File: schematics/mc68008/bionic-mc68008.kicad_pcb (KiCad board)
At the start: 2 copper layers, 66 x 71.1 mm, 16 parts, among them J1 Bionic-P135, J1 BionicConnector, J2 Bionic-P245, U1 MC68008P, U2 74HCT126, U3 74HCT541, U4 74HCT541, U5 11AA010-I/TO

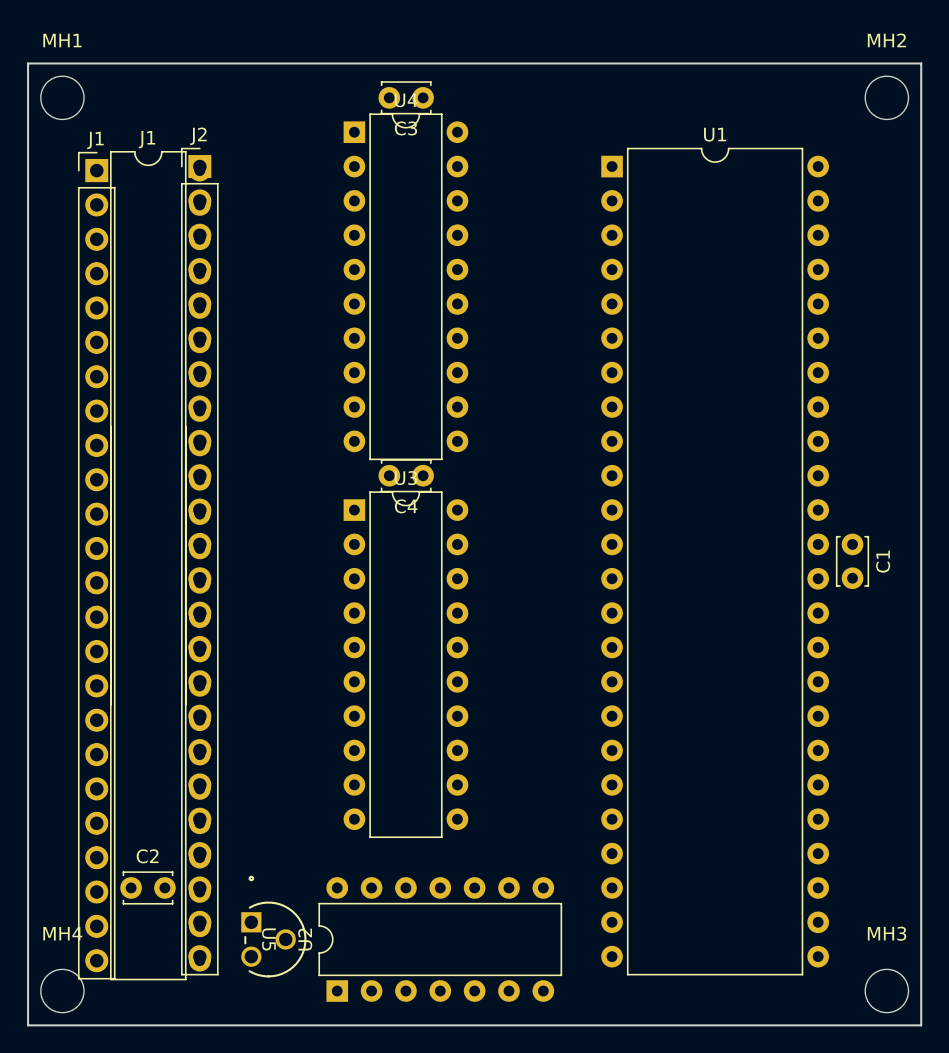
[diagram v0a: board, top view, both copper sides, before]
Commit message: [WIP] [MC68008] Update schematics
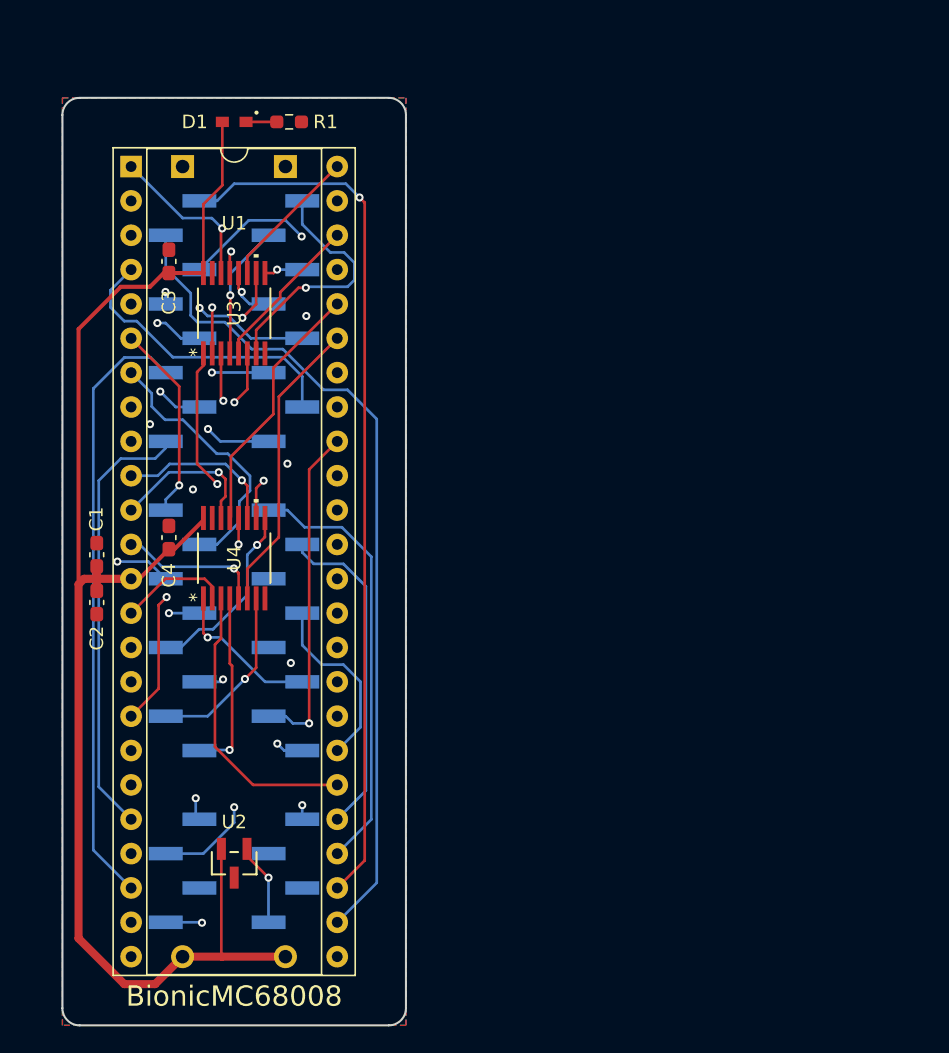
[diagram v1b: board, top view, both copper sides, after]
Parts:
- removed the J1 at (103.5, 75.4) (x2)
- removed MH1, MH2, MH3, MH4: MountingHole_3.2mm_M3, MountingHole:MountingHole_3.2mm_M3
- removed U5: 11AA010-I/TO, microchip:TO-92_MC_MCH
- added D1: CSL1901UW1, rhom:LED_CSL1901UW1_ROM-M, F.Cu at (113.7, 71.8)
- added J1: Bionic-P135, bionic:Bionic-P135_SMT, B.Cu at (109.9, 104.3)
- added R1: 1.6k, Resistor_SMD:R_0603_1608Metric_Pad0.98x0.95mm_HandSolder, F.Cu at (117.8, 71.8)
- C1, C3, C4: footprint Capacitor_THT:C_Disc_D3.4mm_W2.1mm_P2.50mm -> Capacitor_SMD:C_0603_1608Metric_Pad1.08x0.95mm_HandSolder
- C2: value 0.1u -> 22u; footprint Capacitor_THT:C_Disc_D3.4mm_W2.1mm_P2.50mm -> Capacitor_SMD:C_0603_1608Metric_Pad1.08x0.95mm_HandSolder
- J2: footprint connector:Bionic-P245_Vertical -> bionic:Bionic-P245_SMT; moved to B.Cu
- U1: footprint Package_DIP:DIP-48_W15.24mm -> bionic:DIP-48_W15.24mm_Socket
- U2: value 74HCT126 -> 11AA010-I/TT; footprint Package_DIP:DIP-14_W7.62mm -> microchip:SOT-23_MC_MCH-M
- U3, U4: value 74HCT541 -> 74AHCT157; footprint Package_DIP:DIP-20_W7.62mm -> ti:PW16-M
- moved C1 55.9 mm to (103.5, 103.8), turned to 90 degrees
- moved U1 35.6 mm to (106.1, 75.1)
- moved U4 32.7 mm to (113.7, 104.0), turned to 90 degrees
- moved J2 29.9 mm to (117.5, 104.3), turned to 180 degrees
- moved C3 22.3 mm to (108.9, 82.1), turned to 90 degrees
- moved C2 21.3 mm to (103.5, 107.3), turned to -90 degrees
- moved C4 19.3 mm to (108.9, 102.5), turned to 90 degrees
- moved U3 17.1 mm to (113.7, 85.9), turned to 90 degrees
- moved U2 12.1 mm to (113.7, 126.6), turned to 180 degrees
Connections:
- net Net-(U1-A17) renamed /A17
- J2 pad 28: /P55 -> unconnected-(J2-P55-Pad28)
- J2 pad 34: /P44 -> unconnected-(J2-P44-Pad34)
- J2 pad 36: /P42 -> unconnected-(J2-P42-Pad36)
- U1 pad 1: /P23 -> /A3
- U1 pad 10: Net-(U1-A12) -> /A12
- U1 pad 11: Net-(U1-A13) -> /A13
- U1 pad 12: Net-(U1-A14) -> /A14
- U1 pad 14: Net-(U1-A15) -> /A15
- U1 pad 16: Net-(U1-A16) -> /A16
- U1 pad 18: Net-(U1-A18) -> /A18
- U1 pad 19: Net-(U1-A19) -> /A19
- U1 pad 29: /P50 -> /P41
- U1 pad 30: /P41 -> /FC3
- U1 pad 31: /P52 -> /P43
- U1 pad 32: /P44 -> unconnected-(U1-~{BG}-Pad32)
- U1 pad 33: /P47 -> VCC
- U1 pad 34: Net-(U1-CLK) -> /P47
- U1 pad 36: /P51 -> /P54
- U1 pad 40: /P45 -> /P46
- U1 pad 41: /P43 -> /P51
- U1 pad 42: /P42 -> /P50
- U1 pad 43: Net-(U1-FC2) -> /FC2
- U1 pad 44: Net-(U1-FC1) -> /FC1
- U1 pad 45: Net-(U1-FC0) -> /FC0
- U1 pad 46: /P20 -> /A0
- U1 pad 47: /P21 -> /A1
- U1 pad 48: /P22 -> /A2
- U1 pad 6: Net-(U1-A8) -> /P30
- U1 pad 7: Net-(U1-A9) -> /P31
- U1 pad 8: Net-(U1-A10) -> /P32
- U1 pad 9: Net-(U1-A11) -> /P33
- U2 pad 1: VCC -> Net-(J2-P57)
- U2 pad 2: /P46 -> VCC
- U2 pad 3: Net-(U1-CLK) -> GND
- U3 pad 1: /P55 -> /P45
- U3 pad 10: GND -> /A18
- U3 pad 11: unconnected-(U3-Y7-Pad11) -> /A2
- U3 pad 12: /P36 -> /P23
- U3 pad 13: /P35 -> /A19
- U3 pad 14: /P34 -> /A3
- U3 pad 15: /P33 -> GND
- U3 pad 16: /P32 -> VCC
- U3 pad 2: Net-(U1-A16) -> /A1
- U3 pad 4: Net-(U1-A18) -> /P21
- U3 pad 5: Net-(U1-A19) -> /A0
- U3 pad 6: Net-(U1-FC0) -> /A16
- U3 pad 7: Net-(U1-FC1) -> /P20
- U3 pad 8: Net-(U1-FC2) -> GND
- U3 pad 9: GND -> /P22
- U4 pad 1: /P54 -> /P45
- U4 pad 10: GND -> /FC0
- U4 pad 11: /P37 -> /A12
- U4 pad 12: /P36 -> /P35
- U4 pad 13: /P35 -> /FC1
- U4 pad 14: /P34 -> /A13
- U4 pad 15: /P33 -> GND
- U4 pad 16: /P32 -> VCC
- U4 pad 2: Net-(U1-A8) -> /A15
- U4 pad 3: Net-(U1-A9) -> /FC3
- U4 pad 4: Net-(U1-A10) -> /P37
- U4 pad 5: Net-(U1-A11) -> /A14
- U4 pad 6: Net-(U1-A12) -> /FC2
- U4 pad 7: Net-(U1-A13) -> /P36
- U4 pad 8: Net-(U1-A14) -> GND
- U4 pad 9: Net-(U1-A15) -> /P34
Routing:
- net VCC: track 0.00 -> 128.3 mm
- net /P12: track 0.00 -> 67.3 mm, vias 0 -> 1
- net /P10: track 0.00 -> 64.8 mm, vias 0 -> 1
- net /P11: track 0.00 -> 62.0 mm
- net /P13: track 0.00 -> 56.0 mm, vias 0 -> 1
- net /P14: track 0.00 -> 52.2 mm, vias 0 -> 1
- net /A19: track 0.00 -> 45.3 mm, vias 0 -> 1
- net /P15: track 0.00 -> 44.9 mm
- net /P16: track 0.00 -> 42.0 mm, vias 0 -> 1
- net /P51: track 0.00 -> 39.9 mm, vias 0 -> 1
- net /A18: track 0.00 -> 39.1 mm, vias 0 -> 1
- net /P50: track 0.00 -> 37.5 mm, vias 0 -> 1
- net /P53: track 0.00 -> 34.8 mm, vias 0 -> 1
- net /P45: track 0.00 -> 33.5 mm, vias 0 -> 2
- net /P17: track 0.00 -> 32.5 mm
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- added copper zone on B.Cu, net GND
- added copper zone on F.Cu, net GND
- added copper zone on In1.Cu, net GND
- added copper zone on In2.Cu, net GND
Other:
- board size 66 x 71.1 mm -> 25.4 x 68.6 mm
- copper layers 2 -> 4
- rule pad_to_mask_clearance: 0.051 -> 0
- board text added: "BionicMC68008"
- board text added: "JLCJLCJLCJLC"
- board text added: "Rev. 2"
